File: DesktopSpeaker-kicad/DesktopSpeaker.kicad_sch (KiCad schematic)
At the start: 9 parts, among them J1 USB_C_Receptacle_USB2.0_16P, J2 HEAD_OUT, J3 AUX_IN, U10 TPA6132A2RTER, U6 TAS5825MRHBR, U7 TAS5825MRHBR, U8 TS5A23157DGSR, U9 TS5A23157DGSR

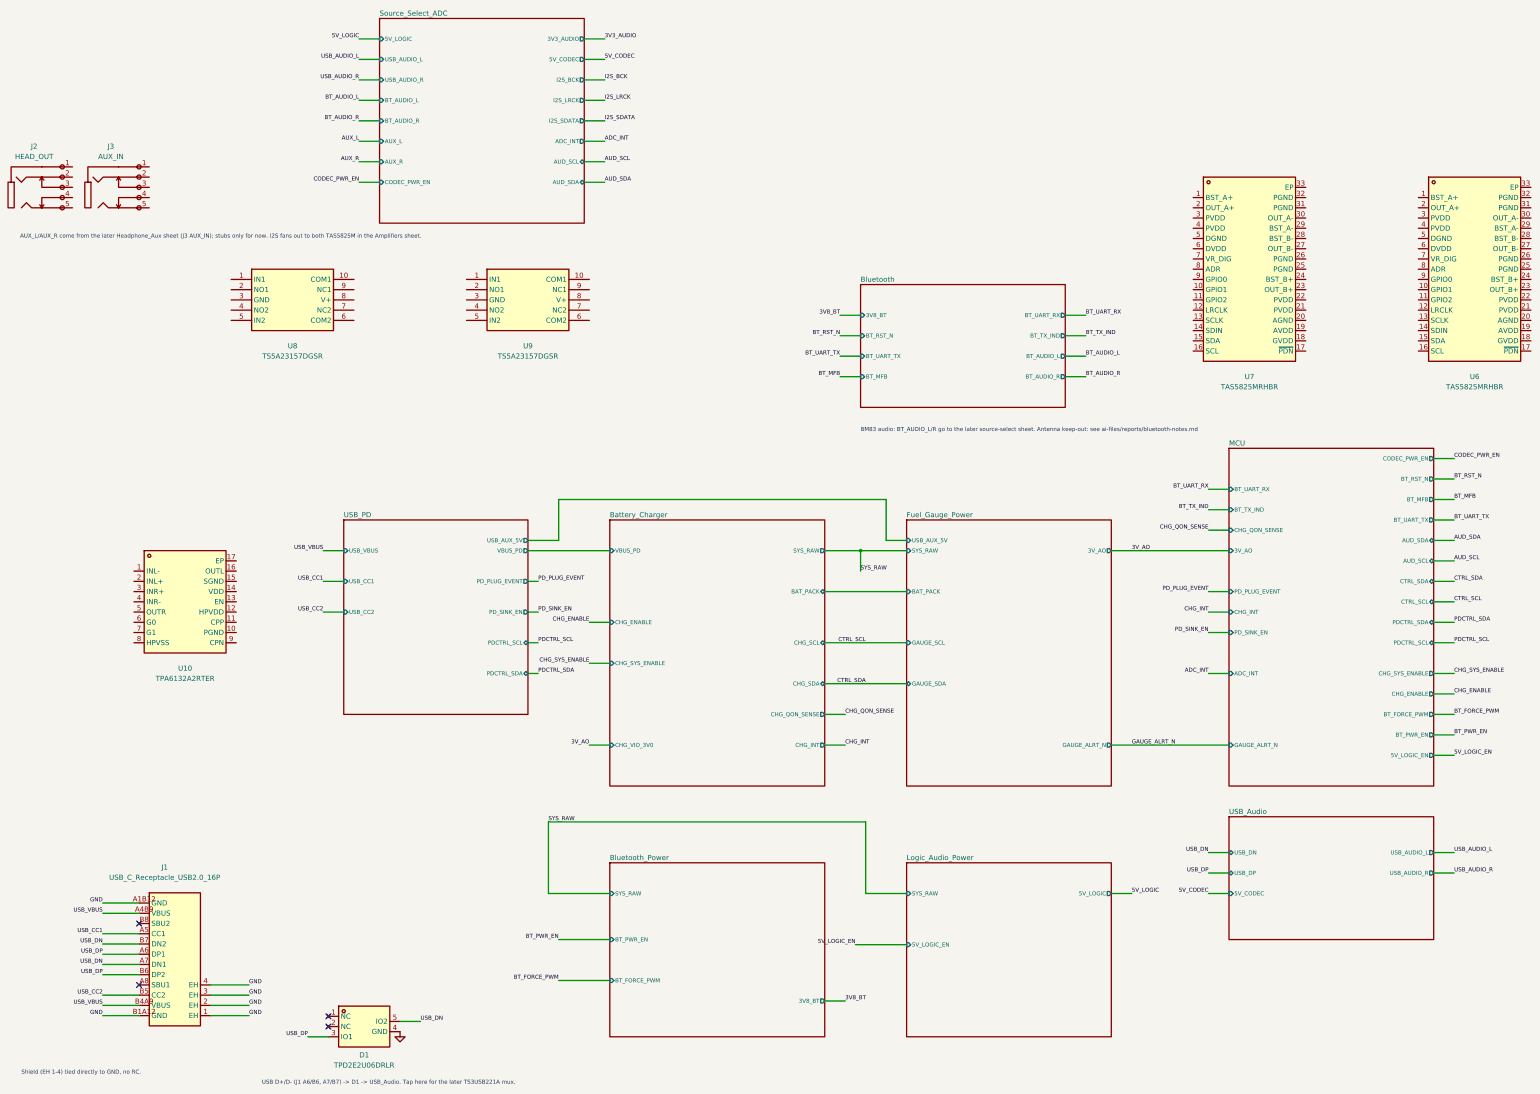
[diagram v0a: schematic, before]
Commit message: Capture Headphone_Aux sheet (TS5A23157 mux, TPA6132A2, jacks) and wire MCU headphone signals
Co-Authored-By: Claude Sonnet 5.5 <noreply@anthropic.com>
Claude-Session: https://claude.ai/code/session_01N5RHheWSjDFDPbKVD5YVeJ
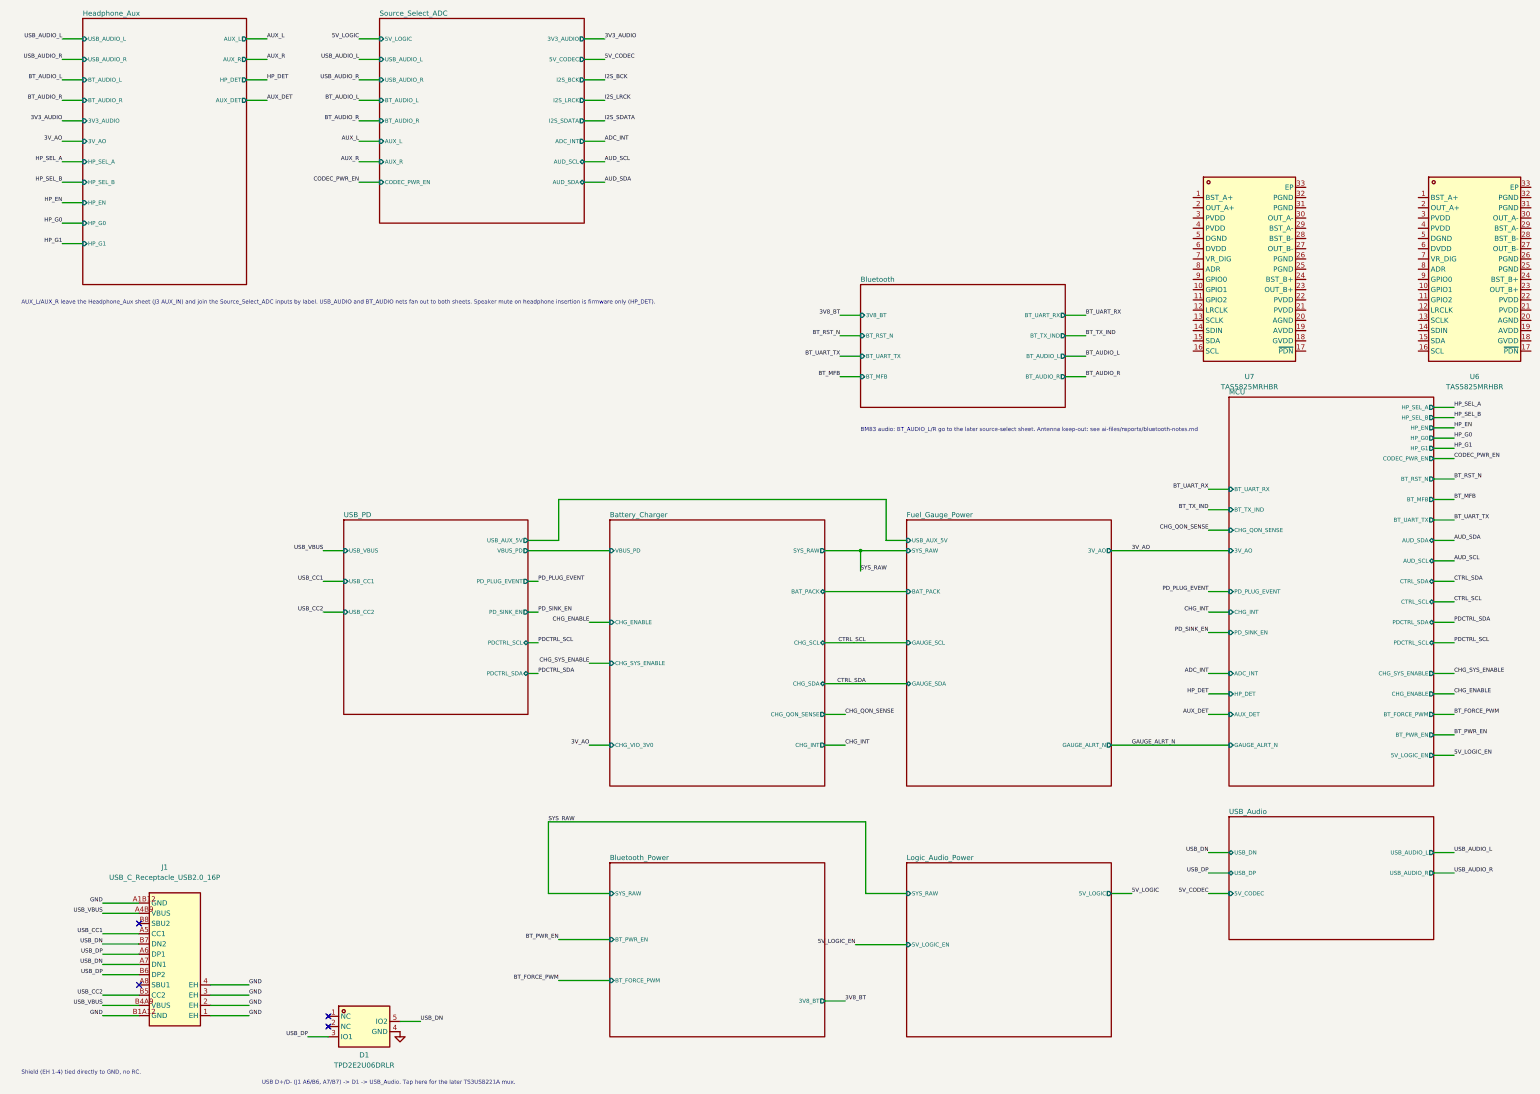
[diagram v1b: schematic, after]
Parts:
- removed J2: HEAD_OUT, DesktopSpeaker:PJ-307, symbol PJ-307:PJ-307
- removed J3: AUX_IN, DesktopSpeaker:PJ-307, symbol PJ-307:PJ-307
- removed U10: TPA6132A2RTER, DesktopSpeaker:TPA6132A2RTER, symbol TPA6132A2RTER:TPA6132A2RTER
- removed U8, U9: TS5A23157DGSR, DesktopSpeaker:TS5A23157DGSR, symbol TS5A23157DGSR:TS5A23157DGSR
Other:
- added sheet Headphone_Aux (Headphone_Aux.kicad_sch)
- sheet MCU ports: added AUX_DET, HP_DET, HP_EN, HP_G0, HP_G1, HP_SEL_A, HP_SEL_B; removed none
- note added: "AUX_L/AUX_R leave the Headphone_Aux sheet (J3 AUX_IN) and join the Source_Select_ADC inputs by label. USB_AUDIO and BT_AUDIO nets fan out to both sheets. Speaker mute on headphone insertion is firmware only (HP_DET)."
- note removed: "AUX_L/AUX_R come from the later Headphone_Aux sheet (J3 AUX_IN); stubs only for now. I2S fans out to both TAS5825M in the Amplifiers sheet."

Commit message: Capture Amplifiers sheet (TPS61088 boost, TAS5825M x2, speaker outputs); correct PBTL pairing
Co-Authored-By: Claude Sonnet 5.5 <noreply@anthropic.com>
Claude-Session: https://claude.ai/code/session_01N5RHheWSjDFDPbKVD5YVeJ
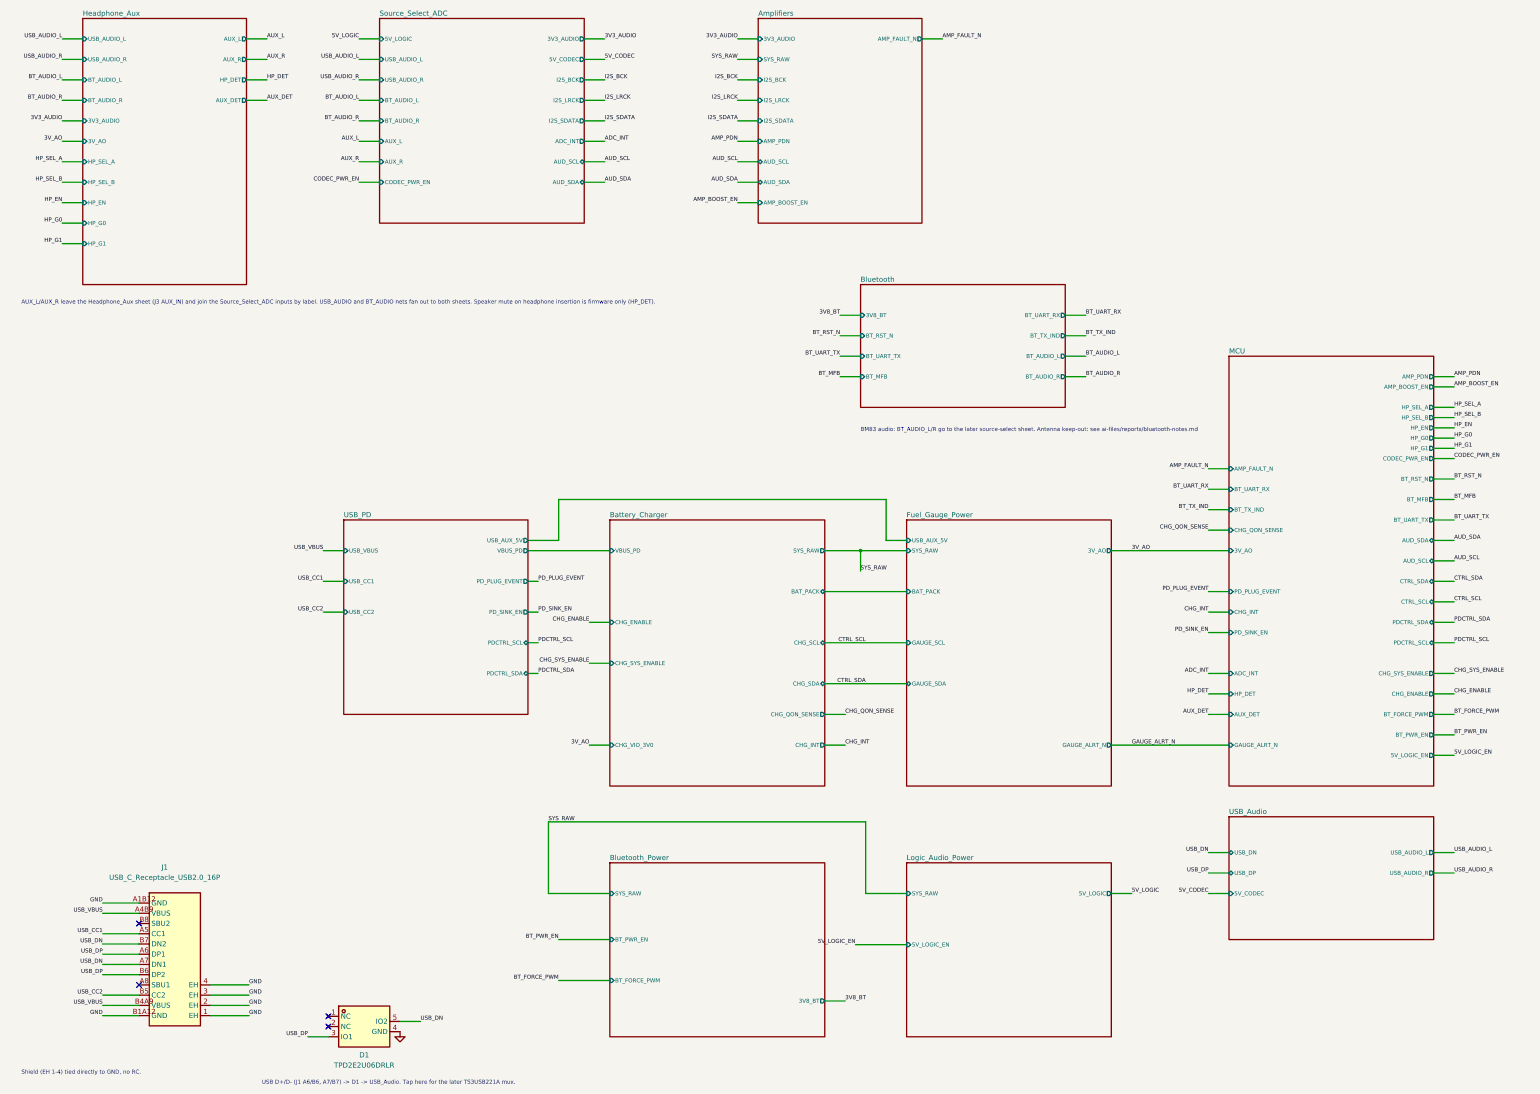
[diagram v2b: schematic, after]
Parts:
- removed U6, U7: TAS5825MRHBR, DesktopSpeaker:TAS5825MRHBR, symbol TAS5825MRHBR:TAS5825MRHBR
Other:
- added sheet Amplifiers (Amplifiers.kicad_sch)
- sheet MCU ports: added AMP_BOOST_EN, AMP_FAULT_N, AMP_PDN; removed none

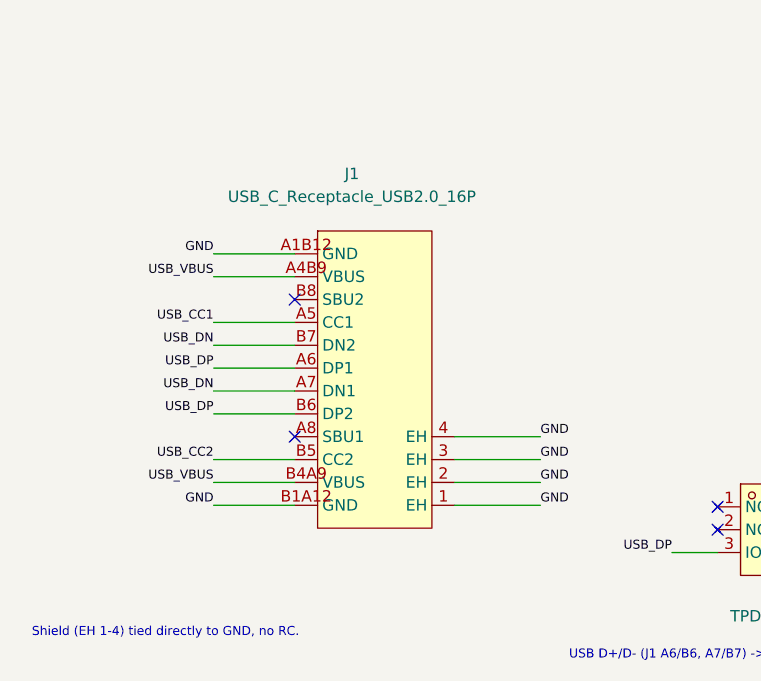
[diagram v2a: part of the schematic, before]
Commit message: Routing R6a-R6m adopted into project board; ERC cleanup, MCU pin swaps, C241 2.2uF, SW100 footprint fix, reviews and helpers
Co-Authored-By: Claude Sonnet 5.5 <noreply@anthropic.com>
Claude-Session: https://claude.ai/code/session_016fe4xPJbEE2SjGafuyNLjb
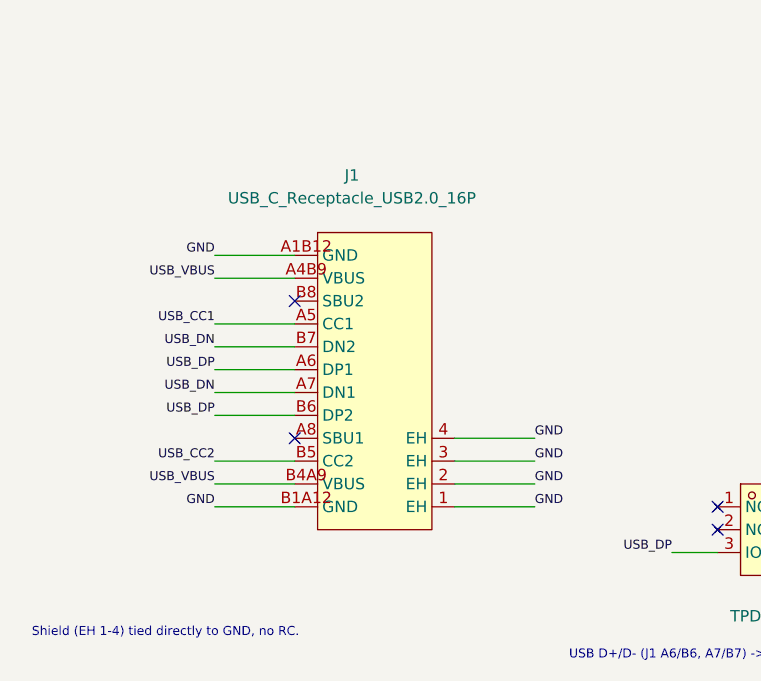
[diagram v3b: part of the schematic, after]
